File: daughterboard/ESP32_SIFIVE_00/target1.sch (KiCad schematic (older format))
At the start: 34 parts, among them IC1 W25X40CLSNIG, U1 ESP32-S2

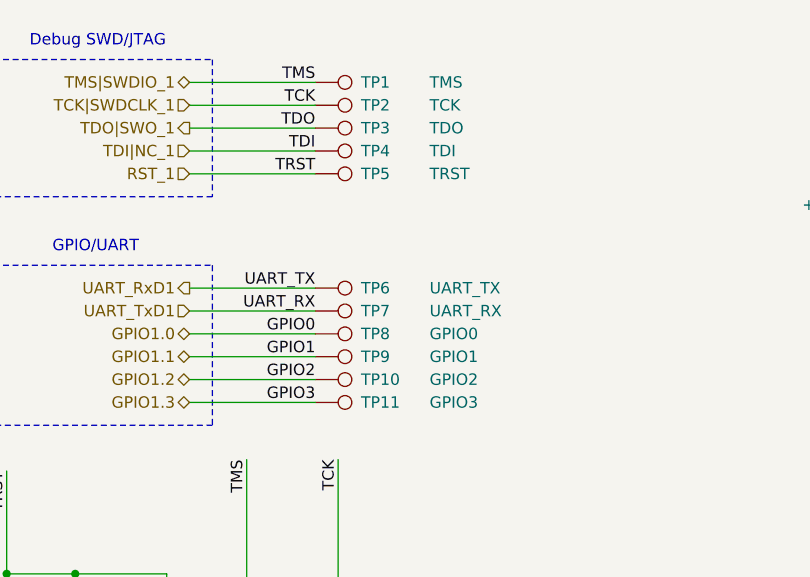
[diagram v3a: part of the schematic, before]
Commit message: started with esp32/sifive layout
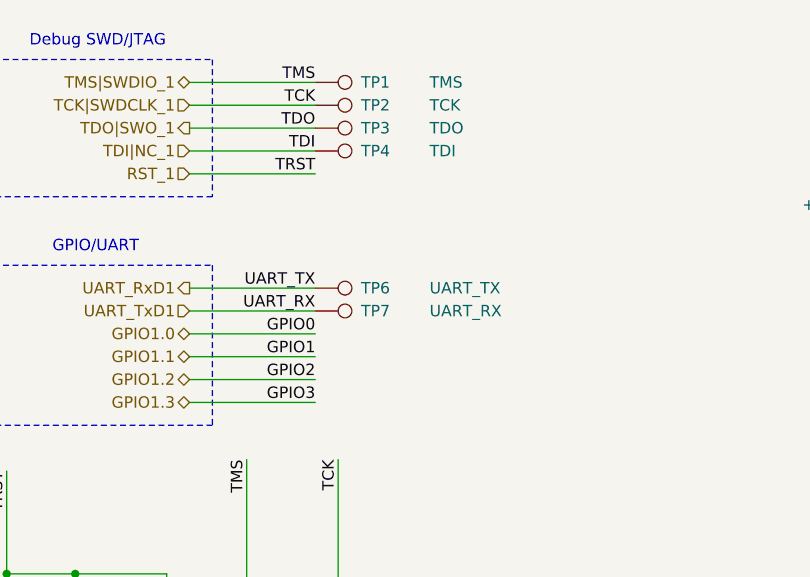
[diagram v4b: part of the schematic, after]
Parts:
- removed TP10: GPIO2, symbol Connector:TestPoint
- removed TP11: GPIO3, symbol Connector:TestPoint
- removed TP5: TRST, symbol Connector:TestPoint
- removed TP8: GPIO0, symbol Connector:TestPoint
- removed TP9: GPIO1, symbol Connector:TestPoint
- C1, C10, C11, C12, C2, C3, C4, C5, C6, C7, C8, C9: footprint (none) -> Capacitor_SMD:C_0603_1608Metric_Pad1.05x0.95mm_HandSolder
- JP1, JP2: footprint (none) -> Jumper:SolderJumper-2_P1.3mm_Open_TrianglePad1.0x1.5mm
- R1, R2, R3, R4, R5, R6, R7: footprint (none) -> Resistor_SMD:R_0603_1608Metric_Pad1.05x0.95mm_HandSolder
- TP1, TP2, TP3, TP4, TP6, TP7: footprint (none) -> TestPoint:TestPoint_Pad_1.0x1.0mm
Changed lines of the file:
@@
 F 0 "C2" H 3942 7296 50  0000 L CNN
 F 1 "1u" H 3942 7205 50  0000 L CNN
-F 2 "" H 3850 7250 50  0001 C CNN
+F 2 "Capacitor_SMD:C_0603_1608Metric_Pad1.05x0.95mm_HandSolder" H 3850 7250 50  0001 C CNN
 F 3 "~" H 3850 7250 50  0001 C CNN
 	1    3850 7250
@@
 F 0 "C3" H 4242 7296 50  0000 L CNN
 F 1 "100n" H 4242 7205 50  0000 L CNN
-F 2 "" H 4150 7250 50  0001 C CNN
+F 2 "Capacitor_SMD:C_0603_1608Metric_Pad1.05x0.95mm_HandSolder" H 4150 7250 50  0001 C CNN
 F 3 "~" H 4150 7250 50  0001 C CNN
 	1    4150 7250
@@
 F 0 "R4" H 4659 7046 50  0000 L CNN
 F 1 "10k" H 4659 6955 50  0000 L CNN
-F 2 "" H 4600 7000 50  0001 C CNN
+F 2 "Resistor_SMD:R_0603_1608Metric_Pad1.05x0.95mm_HandSolder" H 4600 7000 50  0001 C CNN
 F 3 "~" H 4600 7000 50  0001 C CNN
 	1    4600 7000
@@
 F 0 "R3" H 2309 4146 50  0000 L CNN
 F 1 "10k" H 2309 4055 50  0000 L CNN
-F 2 "" H 2250 4100 50  0001 C CNN
+F 2 "Resistor_SMD:R_0603_1608Metric_Pad1.05x0.95mm_HandSolder" H 2250 4100 50  0001 C CNN
 F 3 "~" H 2250 4100 50  0001 C CNN
 	1    2250 4100
@@
 F 0 "R2" H 1909 4146 50  0000 L CNN
 F 1 "10k" H 1909 4055 50  0000 L CNN
-F 2 "" H 1850 4100 50  0001 C CNN
+F 2 "Resistor_SMD:R_0603_1608Metric_Pad1.05x0.95mm_HandSolder" H 1850 4100 50  0001 C CNN
 F 3 "~" H 1850 4100 50  0001 C CNN
 	1    1850 4100
@@
 F 0 "R1" H 859 4146 50  0000 L CNN
 F 1 "100k" H 859 4055 50  0000 L CNN
-F 2 "" H 800 4100 50  0001 C CNN
+F 2 "Resistor_SMD:R_0603_1608Metric_Pad1.05x0.95mm_HandSolder" H 800 4100 50  0001 C CNN
 F 3 "~" H 800 4100 50  0001 C CNN
 	1    800  4100
@@
 F 0 "JP2" V 1454 4168 50  0000 L CNN
 F 1 "NRST" V 1545 4168 50  0000 L CNN
-F 2 "" H 1500 4100 50  0001 C CNN
+F 2 "Jumper:SolderJumper-2_P1.3mm_Open_TrianglePad1.0x1.5mm" H 1500 4100 50  0001 C CNN
 F 3 "~" H 1500 4100 50  0001 C CNN
 	1    1500 4100
@@
 F 0 "C1" H 1192 4146 50  0000 L CNN
 F 1 "100n" H 1192 4055 50  0000 L CNN
-F 2 "" H 1100 4100 50  0001 C CNN
+F 2 "Capacitor_SMD:C_0603_1608Metric_Pad1.05x0.95mm_HandSolder" H 1100 4100 50  0001 C CNN
 F 3 "~" H 1100 4100 50  0001 C CNN
 	1    1100 4100
@@
 F 0 "C4" H 7392 1696 50  0000 L CNN
 F 1 "10u" H 7392 1605 50  0000 L CNN
-F 2 "" H 7300 1650 50  0001 C CNN
+F 2 "Capacitor_SMD:C_0603_1608Metric_Pad1.05x0.95mm_HandSolder" H 7300 1650 50  0001 C CNN
 F 3 "~" H 7300 1650 50  0001 C CNN
 	1    7300 1650
@@
 F 0 "C5" H 7792 1696 50  0000 L CNN
 F 1 "1u" H 7792 1605 50  0000 L CNN
-F 2 "" H 7700 1650 50  0001 C CNN
+F 2 "Capacitor_SMD:C_0603_1608Metric_Pad1.05x0.95mm_HandSolder" H 7700 1650 50  0001 C CNN
 F 3 "~" H 7700 1650 50  0001 C CNN
 	1    7700 1650
@@
 F 0 "C6" H 8142 1696 50  0000 L CNN
 F 1 "100n" H 8142 1605 50  0000 L CNN
-F 2 "" H 8050 1650 50  0001 C CNN
+F 2 "Capacitor_SMD:C_0603_1608Metric_Pad1.05x0.95mm_HandSolder" H 8050 1650 50  0001 C CNN
 F 3 "~" H 8050 1650 50  0001 C CNN
 	1    8050 1650
@@
 F 0 "C7" H 8542 1696 50  0000 L CNN
 F 1 "100n" H 8542 1605 50  0000 L CNN
-F 2 "" H 8450 1650 50  0001 C CNN
+F 2 "Capacitor_SMD:C_0603_1608Metric_Pad1.05x0.95mm_HandSolder" H 8450 1650 50  0001 C CNN
 F 3 "~" H 8450 1650 50  0001 C CNN
 	1    8450 1650
@@
 F 0 "C8" H 8942 1696 50  0000 L CNN
 F 1 "100n" H 8942 1605 50  0000 L CNN
-F 2 "" H 8850 1650 50  0001 C CNN
+F 2 "Capacitor_SMD:C_0603_1608Metric_Pad1.05x0.95mm_HandSolder" H 8850 1650 50  0001 C CNN
 F 3 "~" H 8850 1650 50  0001 C CNN
 	1    8850 1650
@@
 F 0 "C9" H 9342 1696 50  0000 L CNN
 F 1 "100n" H 9342 1605 50  0000 L CNN
-F 2 "" H 9250 1650 50  0001 C CNN
+F 2 "Capacitor_SMD:C_0603_1608Metric_Pad1.05x0.95mm_HandSolder" H 9250 1650 50  0001 C CNN
 F 3 "~" H 9250 1650 50  0001 C CNN
 	1    9250 1650
@@
 F 0 "C10" H 9742 1696 50  0000 L CNN
 F 1 "100n" H 9742 1605 50  0000 L CNN
-F 2 "" H 9650 1650 50  0001 C CNN
+F 2 "Capacitor_SMD:C_0603_1608Metric_Pad1.05x0.95mm_HandSolder" H 9650 1650 50  0001 C CNN
 F 3 "~" H 9650 1650 50  0001 C CNN
 	1    9650 1650
@@
 F 0 "C11" H 10192 1696 50  0000 L CNN
 F 1 "100n" H 10192 1605 50  0000 L CNN
-F 2 "" H 10100 1650 50  0001 C CNN
+F 2 "Capacitor_SMD:C_0603_1608Metric_Pad1.05x0.95mm_HandSolder" H 10100 1650 50  0001 C CNN
 F 3 "~" H 10100 1650 50  0001 C CNN
 	1    10100 1650
@@
 F 0 "C12" H 10592 1696 50  0000 L CNN
 F 1 "100n" H 10592 1605 50  0000 L CNN
-F 2 "" H 10500 1650 50  0001 C CNN
+F 2 "Capacitor_SMD:C_0603_1608Metric_Pad1.05x0.95mm_HandSolder" H 10500 1650 50  0001 C CNN
 F 3 "~" H 10500 1650 50  0001 C CNN
 	1    10500 1650
@@
 F 0 "R5" V 4900 2000 50  0000 L CNN
 F 1 "100k" V 4900 2400 50  0000 L CNN
-F 2 "" H 4950 2250 50  0001 C CNN
+F 2 "Resistor_SMD:R_0603_1608Metric_Pad1.05x0.95mm_HandSolder" H 4950 2250 50  0001 C CNN
 F 3 "~" H 4950 2250 50  0001 C CNN
 	1    4950 2250
@@
 F 0 "R7" V 8350 2300 50  0000 L CNN
 F 1 "100k" V 8350 2700 50  0000 L CNN
-F 2 "" H 8400 2550 50  0001 C CNN
+F 2 "Resistor_SMD:R_0603_1608Metric_Pad1.05x0.95mm_HandSolder" H 8400 2550 50  0001 C CNN
 F 3 "~" H 8400 2550 50  0001 C CNN
 	1    8400 2550
@@
 F 0 "R6" V 8350 2000 50  0000 L CNN
 F 1 "100k" V 8350 2400 50  0000 L CNN
-F 2 "" H 8400 2250 50  0001 C CNN
+F 2 "Resistor_SMD:R_0603_1608Metric_Pad1.05x0.95mm_HandSolder" H 8400 2250 50  0001 C CNN
 F 3 "~" H 8400 2250 50  0001 C CNN
 	1    8400 2250
@@
 F 0 "JP1" H 850 5175 50  0000 C CNN
 F 1 "BOOT" H 850 5266 50  0000 C CNN
-F 2 "" H 850 5400 50  0001 C CNN
+F 2 "Jumper:SolderJumper-2_P1.3mm_Open_TrianglePad1.0x1.5mm" H 850 5400 50  0001 C CNN
 F 3 "~" H 850 5400 50  0001 C CNN
 	1    850  5400
@@
 F 0 "TP1" V 2150 1900 50  0000 L CNN
 F 1 "TMS" V 2150 2200 50  0000 L CNN
-F 2 "" H 2350 1700 50  0001 C CNN
+F 2 "TestPoint:TestPoint_Pad_1.0x1.0mm" H 2350 1700 50  0001 C CNN
 F 3 "~" H 2350 1700 50  0001 C CNN
 	1    2150 1700
@@
 F 0 "TP2" V 2150 2000 50  0000 L CNN
 F 1 "TCK" V 2150 2300 50  0000 L CNN
-F 2 "" H 2350 1800 50  0001 C CNN
+F 2 "TestPoint:TestPoint_Pad_1.0x1.0mm" H 2350 1800 50  0001 C CNN
 F 3 "~" H 2350 1800 50  0001 C CNN
 	1    2150 1800
@@
 F 0 "TP3" V 2150 2100 50  0000 L CNN
 F 1 "TDO" V 2150 2400 50  0000 L CNN
-F 2 "" H 2350 1900 50  0001 C CNN
+F 2 "TestPoint:TestPoint_Pad_1.0x1.0mm" H 2350 1900 50  0001 C CNN
 F 3 "~" H 2350 1900 50  0001 C CNN
 	1    2150 1900
@@
 F 0 "TP4" V 2150 2200 50  0000 L CNN
 F 1 "TDI" V 2150 2500 50  0000 L CNN
-F 2 "" H 2350 2000 50  0001 C CNN
+F 2 "TestPoint:TestPoint_Pad_1.0x1.0mm" H 2350 2000 50  0001 C CNN
 F 3 "~" H 2350 2000 50  0001 C CNN
 	1    2150 2000
-	0    1    1    0
-$EndComp
-$Comp
-L Connector:TestPoint TP?
-U 1 1 6192681C
-P 2150 2100
-AR Path="/616688D6/6192681C" Ref="TP?"  Part="1"
-AR Path="/61667F91/6192681C" Ref="TP5"  Part="1"
-F 0 "TP5" V 2150 2300 50  0000 L CNN
-F 1 "TRST" V 2150 2600 50  0000 L CNN
-F 2 "" H 2350 2100 50  0001 C CNN
-F 3 "~" H 2350 2100 50  0001 C CNN
-	1    2150 2100
 	0    1    1    0
 $EndComp
@@
 F 0 "TP6" V 2150 2800 50  0000 L CNN
 F 1 "UART_TX" V 2150 3100 50  0000 L CNN
-F 2 "" H 2350 2600 50  0001 C CNN
+F 2 "TestPoint:TestPoint_Pad_1.0x1.0mm" H 2350 2600 50  0001 C CNN
 F 3 "~" H 2350 2600 50  0001 C CNN
 	1    2150 2600
@@
 F 0 "TP7" V 2150 2900 50  0000 L CNN
 F 1 "UART_RX" V 2150 3200 50  0000 L CNN
-F 2 "" H 2350 2700 50  0001 C CNN
+F 2 "TestPoint:TestPoint_Pad_1.0x1.0mm" H 2350 2700 50  0001 C CNN
 F 3 "~" H 2350 2700 50  0001 C CNN
 	1    2150 2700
 	0    1    1    0
 $EndComp
-$Comp
-L Connector:TestPoint TP?
-U 1 1 6192682E
-P 2150 2800
-AR Path="/616688D6/6192682E" Ref="TP?"  Part="1"
-AR Path="/61667F91/6192682E" Ref="TP8"  Part="1"
-F 0 "TP8" V 2150 3000 50  0000 L CNN
-F 1 "GPIO0" V 2150 3300 50  0000 L CNN
-F 2 "" H 2350 2800 50  0001 C CNN
-F 3 "~" H 2350 2800 50  0001 C CNN
-	1    2150 2800
-	0    1    1    0
-$EndComp
-$Comp
-L Connector:TestPoint TP?
-U 1 1 61926834
-P 2150 2900
-AR Path="/616688D6/61926834" Ref="TP?"  Part="1"
-AR Path="/61667F91/61926834" Ref="TP9"  Part="1"
-F 0 "TP9" V 2150 3100 50  0000 L CNN
-F 1 "GPIO1" V 2150 3400 50  0000 L CNN
-F 2 "" H 2350 2900 50  0001 C CNN
-F 3 "~" H 2350 2900 50  0001 C CNN
-	1    2150 2900
-	0    1    1    0
-$EndComp
-$Comp
-L Connector:TestPoint TP?
-U 1 1 6192683A
-P 2150 3000
-AR Path="/616688D6/6192683A" Ref="TP?"  Part="1"
-AR Path="/61667F91/6192683A" Ref="TP10"  Part="1"
-F 0 "TP10" V 2150 3200 50  0000 L CNN
-F 1 "GPIO2" V 2150 3500 50  0000 L CNN
-F 2 "" H 2350 3000 50  0001 C CNN
-F 3 "~" H 2350 3000 50  0001 C CNN
-	1    2150 3000
-	0    1    1    0
-$EndComp
-$Comp
-L Connector:TestPoint TP?
-U 1 1 61926840
-P 2150 3100
-AR Path="/616688D6/61926840" Ref="TP?"  Part="1"
-AR Path="/61667F91/61926840" Ref="TP11"  Part="1"
-F 0 "TP11" V 2150 3300 50  0000 L CNN
-F 1 "GPIO3" V 2150 3600 50  0000 L CNN
-F 2 "" H 2350 3100 50  0001 C CNN
-F 3 "~" H 2350 3100 50  0001 C CNN
-	1    2150 3100
-	0    1    1    0
-$EndComp
